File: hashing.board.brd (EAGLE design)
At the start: 160 x 100 mm, 131 parts, among them U1 ASIC-1, U10 EPM570GT100C5N, U2 ASIC-1, U3 ASIC-1, U4 ASIC-1, U5 ASIC-1, U6 ASIC-1, U7 ASIC-1, U8 ASIC-1, U9 AT32UC3A1256-AUT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

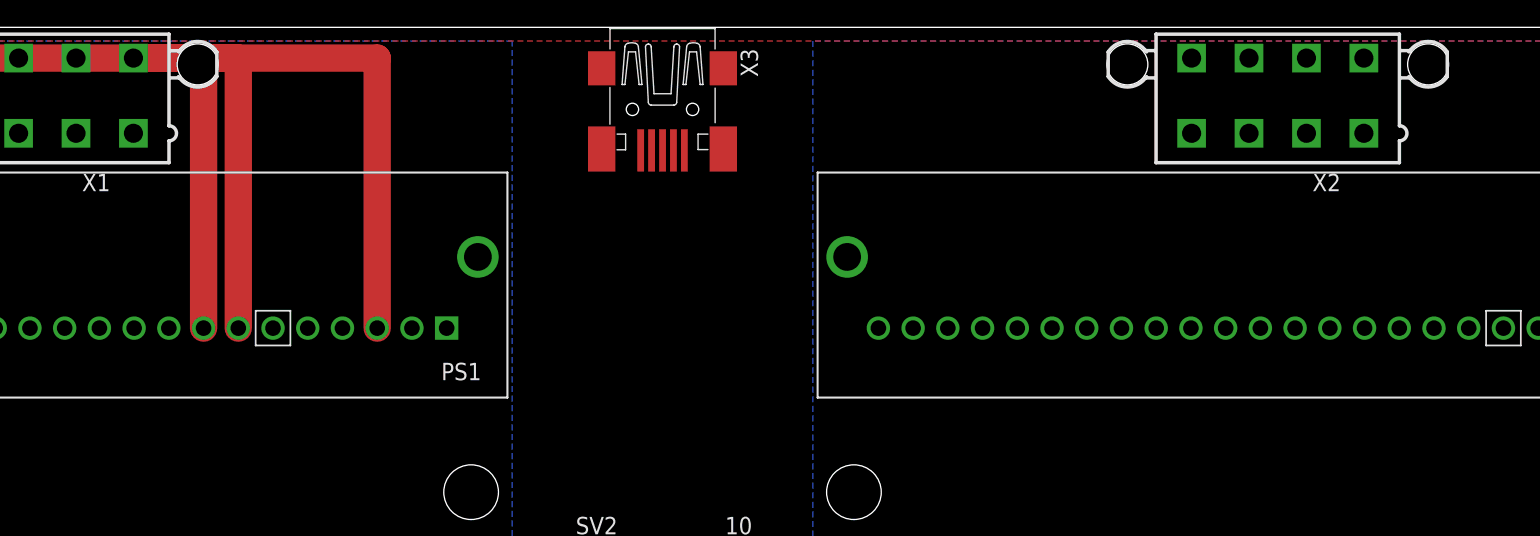
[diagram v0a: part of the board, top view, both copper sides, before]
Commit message: added the 5v and 3.3v power
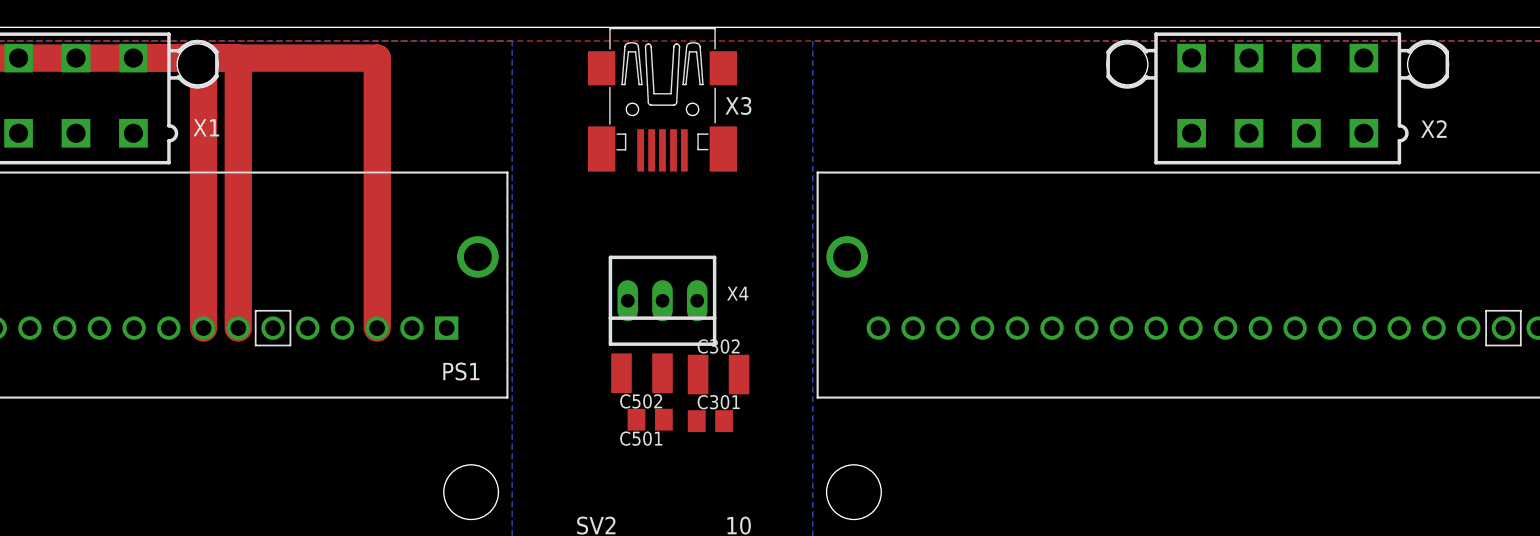
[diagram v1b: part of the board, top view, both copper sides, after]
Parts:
- added C301, C501: (no value), rcl:C0805K
- added C302, C502: (no value), rcl:C1210K
- added X4: 22-23-2031, con-molex:22-23-2031
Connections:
- new net VIN-3.3V: C301.1, C302.1, X4.1
- new net VIN-5.0V: C501.1, C502.1, X4.2
- net GND: now also C301.2, C302.2, C501.2, C502.2, X4.3
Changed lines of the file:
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@@
 <attribute name="OC_FARNELL" value="unknown" x="80" y="60" size="1.778" layer="27" display="off"/>
 </element>
-<element name="X1" library="con-molex" package="5566-8" value="5566-8" x="35" y="95">
+<element name="X1" library="con-molex" package="5566-8" value="5566-8" x="35" y="95" smashed="yes">
 <attribute name="OC_NEWARK" value="unknown" x="35" y="95" size="1.778" layer="27" display="off"/>
 <attribute name="MPN" value="" x="35" y="95" size="1.778" layer="27" display="off"/>
 <attribute name="MF" value="" x="35" y="95" size="1.778" layer="27" display="off"/>
 <attribute name="OC_FARNELL" value="unknown" x="35" y="95" size="1.778" layer="27" display="off"/>
+<attribute name="NAME" x="45.64" y="92.015" size="1.27" layer="25"/>
 </element>
-<element name="X2" library="con-molex" package="5566-8" value="5566-8" x="125" y="95">
+<element name="X2" library="con-molex" package="5566-8" value="5566-8" x="125" y="95" smashed="yes">
 <attribute name="OC_NEWARK" value="unknown" x="125" y="95" size="1.778" layer="27" display="off"/>
 <attribute name="MPN" value="" x="125" y="95" size="1.778" layer="27" display="off"/>
 <attribute name="MF" value="" x="125" y="95" size="1.778" layer="27" display="off"/>
 <attribute name="OC_FARNELL" value="unknown" x="125" y="95" size="1.778" layer="27" display="off"/>
+<attribute name="NAME" x="135.44" y="91.915" size="1.27" layer="25"/>
 </element>
-<element name="X3" library="con-cypressindustries" package="32005-301" value="MINI-USB-32005-301" x="80" y="94" rot="R270">
+<element name="X3" library="con-cypressindustries" package="32005-301" value="MINI-USB-32005-301" x="80" y="94" smashed="yes" rot="R270">
 <attribute name="OC_NEWARK" value="unknown" x="80" y="94" size="1.778" layer="27" rot="R270" display="off"/>
 <attribute name="MPN" value="" x="80" y="94" size="1.778" layer="27" rot="R270" display="off"/>
 <attribute name="MF" value="" x="80" y="94" size="1.778" layer="27" rot="R270" display="off"/>
 <attribute name="OC_FARNELL" value="unknown" x="80" y="94" size="1.778" layer="27" rot="R270" display="off"/>
+<attribute name="NAME" x="84.555" y="93.615" size="1.27" layer="25"/>
 </element>
 <element name="WHAT_VOLTAGE" library="rcl" package="R0402" value="" x="-9.1" y="-95.6"/>
+<element name="X4" library="con-molex" package="22-23-2031" value="22-23-2031" x="80" y="80" smashed="yes" rot="R180">
+<attribute name="OC_NEWARK" value="30C0862" x="80" y="80" size="1.778" layer="27" rot="R180" display="off"/>
+<attribute name="MPN" value="22-23-2031" x="80" y="80" size="1.778" layer="27" rot="R180" display="off"/>
+<attribute name="MF" value="MOLEX" x="80" y="80" size="1.778" layer="27" rot="R180" display="off"/>
+<attribute name="OC_FARNELL" value="1462950" x="80" y="80" size="1.778" layer="27" rot="R180" display="off"/>
+<attribute name="NAME" x="84.69" y="80.01" size="1.016" layer="25" ratio="10"/>
+</element>
+<element name="C502" library="rcl" package="C1210K" value="" x="78.5" y="74.7" rot="R180"/>
+<element name="C302" library="rcl" package="C1210K" value="" x="84.1" y="74.6"/>
+<element name="C301" library="rcl" package="C0805K" value="" x="83.5" y="71.2"/>
+<element name="C501" library="rcl" package="C0805K" value="" x="79.1" y="71.3" rot="R180"/>
 </elements>
 <signals>
@@
 <contactref element="SV2" pad="2"/>
 <contactref element="SV2" pad="10"/>
+<contactref element="X4" pad="3"/>
+<contactref element="C502" pad="2"/>
+<contactref element="C501" pad="2"/>
+<contactref element="C302" pad="2"/>
+<contactref element="C301" pad="2"/>
 <wire x1="127.1" y1="97.75" x2="131.3" y2="97.75" width="0" layer="19" extent="1-1"/>
 <wire x1="122.9" y1="97.75" x2="127.1" y2="97.75" width="0" layer="19" extent="1-1"/>
@@
 <wire x1="103.41" y1="78" x2="108.49" y2="78" width="0" layer="19" extent="1-1"/>
 <wire x1="98.33" y1="78" x2="103.41" y2="78" width="0" layer="19" extent="1-1"/>
-<wire x1="85.08" y1="61.27" x2="98.33" y2="78" width="0" layer="19" extent="1-1"/>
+<wire x1="85.6" y1="74.6" x2="98.33" y2="78" width="0" layer="19" extent="1-1"/>
+<wire x1="84.5" y1="71.2" x2="85.6" y2="74.6" width="0" layer="19" extent="1-1"/>
+<wire x1="78.1" y1="71.3" x2="84.5" y2="71.2" width="0" layer="19" extent="1-1"/>
+<wire x1="77" y1="74.7" x2="78.1" y2="71.3" width="0" layer="19" extent="1-1"/>
+<wire x1="77.46" y1="80" x2="77" y2="74.7" width="0" layer="19" extent="1-1"/>
+<wire x1="85.08" y1="61.27" x2="84.5" y2="71.2" width="0" layer="19" extent="1-1"/>
 <wire x1="84.5" y1="55.25" x2="85.08" y2="61.27" width="0" layer="19" extent="1-1"/>
 <wire x1="83.9878" y1="52.62" x2="84.5" y2="55.25" width="0" layer="19" extent="1-1"/>
@@
 <wire x1="69.85" y1="22" x2="72.38" y2="21.4986" width="0" layer="19" extent="1-1"/>
 <wire x1="69.85" y1="20" x2="69.85" y2="22" width="0" layer="19" extent="1-1"/>
+<wire x1="59.13" y1="78" x2="77" y2="74.7" width="0" layer="19" extent="1-1"/>
+<wire x1="41.35" y1="78" x2="46.43" y2="78" width="0" layer="19" extent="1-1"/>
 <wire x1="110.6" y1="44.6" x2="91.3" y2="43.85" width="0" layer="19" extent="1-1"/>
 <wire x1="111.4" y1="44.6" x2="110.6" y2="44.6" width="0" layer="19" extent="1-1"/>
@@
 <wire x1="48.6" y1="21.4" x2="48.6" y2="22.2" width="0" layer="19" extent="1-1"/>
 <wire x1="49.4" y1="21.4" x2="48.6" y2="21.4" width="0" layer="19" extent="1-1"/>
-<wire x1="59.13" y1="78" x2="74.92" y2="61.27" width="0" layer="19" extent="1-1"/>
-<wire x1="41.35" y1="78" x2="46.43" y2="78" width="0" layer="19" extent="1-1"/>
 <wire x1="4.525" y1="-8.3" x2="20.6" y2="21.4" width="0" layer="19" extent="1-1"/>
 <wire x1="6.275" y1="-11.4" x2="4.525" y2="-8.3" width="0" layer="19" extent="1-1"/>
@@
 <wire x1="-8.45" y1="-95.6" x2="83.9878" y2="37.38" width="0" layer="19" extent="1-1"/>
 </signal>
+<signal name="VIN-5.0V">
+<contactref element="X4" pad="2"/>
+<contactref element="C502" pad="1"/>
+<contactref element="C501" pad="1"/>
+<wire x1="80" y1="74.7" x2="80" y2="80" width="0" layer="19" extent="1-1"/>
+<wire x1="80.1" y1="71.3" x2="80" y2="74.7" width="0" layer="19" extent="1-1"/>
+</signal>
+<signal name="VIN-3.3V">
+<contactref element="X4" pad="1"/>
+<contactref element="C302" pad="1"/>
+<contactref element="C301" pad="1"/>
+<wire x1="82.6" y1="74.6" x2="82.54" y2="80" width="0" layer="19" extent="1-1"/>
+<wire x1="82.5" y1="71.2" x2="82.6" y2="74.6" width="0" layer="19" extent="1-1"/>
+</signal>
 </signals>
